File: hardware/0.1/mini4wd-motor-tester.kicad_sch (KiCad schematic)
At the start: 93 parts, among them J1 USB_C_Receptacle_USB2.0_16P, J2 JST SH, J3 JST SH, M1 Motor_DC, SW1 RA, SW2 RA, SW3 EC11, U1 TLV62130, U2 USBLC6-2SC6, U3 RT9080-33GJ5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

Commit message: add wheel rpm, aux 5V circuits
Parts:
- added C24: 100n, Capacitor_SMD:C_0603_1608Metric, symbol Device:C
- added D3: B5819W, Diode_SMD:D_SOD-123, symbol Device:D_Schottky
- added J4: JST XH, Connector_JST:JST_XH_B2B-XH-A_1x02_P2.50mm_Vertical, symbol Connector_Generic:Conn_01x02
- added Q2: AO3401A, Package_TO_SOT_SMD:SOT-23, symbol Transistor_FET:AO3401A
- added Q3: 2N7002, Package_TO_SOT_SMD:SOT-23, symbol Transistor_FET:Q_NMOS_GSD
- added R25: 22R, Resistor_SMD:R_0603_1608Metric, symbol Device:R
- added R26: 2K2, Resistor_SMD:R_0603_1608Metric, symbol Device:R
- added R27, R28: 10K, Resistor_SMD:R_0603_1608Metric, symbol Device:R
- added RV2: POT_10K, josh-passives-smt:Potentiometer_Bourns_TC33X_Vertical, symbol Device:R_Potentiometer
- added TP12: TP, TestPoint:TestPoint_Pad_D1.0mm, symbol Connector:TestPoint
- added U10: GP2S700HCP, josh-passives-smt:Sharp_GP2S700HCP, symbol Sensor_Proximity:GP2S700HCP
- C1, C23, C3: footprint Capacitor_SMD:C_1206_3216Metric -> Capacitor_SMD:C_0805_2012Metric; LCSC C13585 -> C440198; MPN  CL31A106KBHNNNE -> GRM21BR61H106KE43L; Manufacturer Samsung Electro-Mechanics -> Murata
- C2, C20, C21: Manufacturer FH (Guangdong Fenghua Advanced Tech) -> FH (Guangdong Fenghua Advanced Tech)
- J2, J3: Manufacturer JST Sales America -> JST
- L1: LCSC C3222743 -> C436515; MPN  IHLP1616BZER2R2M5A -> PSPMAA0402-2R2M-ANP; Manufacturer Vishay -> PROD Tech
- U9: footprint Package_SON:WSON-8-1EP_2x2mm_P0.5mm_EP0.9x1.6mm_ThermalVias -> Package_SON:WSON-8-1EP_2x2mm_P0.5mm_EP0.9x1.6mm
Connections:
- net +3V3: now also R26.1, U10.4 (A)
- net +5V: now also Q2.2 (S), R28.2
- net GND: now also C24.2, D3.2 (A), J4.2 (Pin_2), Q3.2 (S), R25.1, R27.2, RV2.3, U10.1
- net AUX_5V_EN: now reaches U5.38 (IO2)
- net AUX_5V_EN: now also Q3.1 (G), R27.1
- net WHEEL_OUT: now reaches U5.39 (IO1)
- net WHEEL_OUT: now also RV2.2, TP12.1
- net RPM_OUT renamed MOTOR_OUT
- new net: Q2.1 (G), Q3.3 (D), R28.1
- new net: C24.1, D3.1 (K), J4.1 (Pin_1), Q2.3 (D)
- new net: R26.2, RV2.1, U10.2
- new net: R25.2, U10.3 (K)
- no-connect marks 21 -> 19
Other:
- note added: "AUX 5V Supply"
- note added: "Motor RPM Counter"
- note added: "Wheel RPM Counter"
- note removed: "RPM Counter"
- moved on the sheet: TP11

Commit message: update motor cutout, provision space for wheel speed tester
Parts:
- R8: value 22K -> 30K; LCSC C31850 -> C22984; MPN  0603WAF2202T5E -> 0603WAF3002T5E
- R9: value 75K -> 100K; LCSC C23242 -> C25803; MPN  0603WAF7502T5E -> 0603WAF1003T5E

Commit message: shrinking board down
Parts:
- removed C18: 1u, Capacitor_SMD:C_0603_1608Metric, symbol Device:C
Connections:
- net TXD: now reaches J2.3 (Pin_3), U5.37 (TXD0)
- net RXD: now reaches J2.4 (Pin_4), U5.36 (RXD0)
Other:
- moved on the sheet: TP10, TP9
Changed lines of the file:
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@@
 	)
 	(junction
-		(at 247.65 31.75)
-		(diameter 0)
-		(color 0 0 0 0)
-	)
-	(junction
 		(at 358.14 208.28)
 		(diameter 0)
@@
 	(wire
 		(pts
+			(xy 199.39 45.72) (xy 209.55 45.72)
+		)
+		(stroke
+			(width 0)
+			(type default)
+		)
+	)
+	(wire
+		(pts
 			(xy 36.83 113.03) (xy 59.69 113.03)
 		)
@@
 	(wire
 		(pts
-			(xy 370.84 49.53) (xy 389.89 49.53)
+			(xy 370.84 49.53) (xy 391.16 49.53)
 		)
 		(stroke
@@
 	(wire
 		(pts
-			(xy 209.55 45.72) (xy 199.39 45.72)
-		)
-		(stroke
-			(width 0)
-			(type default)
-		)
-	)
-	(wire
-		(pts
 			(xy 54.61 35.56) (xy 50.8 35.56)
 		)
@@
 	(wire
 		(pts
-			(xy 370.84 44.45) (xy 389.89 44.45)
+			(xy 370.84 44.45) (xy 391.16 44.45)
 		)
 		(stroke
@@
 	(wire
 		(pts
-			(xy 260.35 31.75) (xy 260.35 34.29)
-		)
-		(stroke
-			(width 0)
-			(type default)
-		)
-	)
-	(wire
-		(pts
 			(xy 73.66 46.99) (xy 73.66 45.72)
 		)
@@
 	(wire
 		(pts
-			(xy 247.65 31.75) (xy 260.35 31.75)
-		)
-		(stroke
-			(width 0)
-			(type default)
-		)
-	)
-	(wire
-		(pts
 			(xy 278.13 196.85) (xy 278.13 198.12)
 		)
@@
 		)
 	)
+	(label "RXD"
+		(at 201.93 48.26 0)
+		(effects
+			(font
+				(size 1.27 1.27)
+				(thickness 0.254)
+				(bold yes)
+			)
+			(justify left bottom)
+		)
+	)
 	(label "I2C_SDA"
 		(at 256.54 71.12 180)
@@
 		)
 	)
+	(label "TXD"
+		(at 201.93 45.72 0)
+		(effects
+			(font
+				(size 1.27 1.27)
+				(thickness 0.254)
+				(bold yes)
+			)
+			(justify left bottom)
+		)
+	)
 	(label "SPI_POCI"
 		(at 256.54 83.82 180)
@@
 	(symbol
 		(lib_id "Connector:TestPoint")
-		(at 389.89 44.45 270)
+		(at 391.16 44.45 270)
 		(mirror x)
 		(unit 1)
@@
 		(dnp no)
 		(property "Reference" "TP9"
-			(at 390.652 43.434 90)
+			(at 391.922 43.434 90)
 			(effects
 				(font
@@
 		)
 		(property "Value" "TP"
-			(at 391.16 45.72 90)
+			(at 392.43 45.72 90)
 			(effects
 				(font
@@
 		)
 		(property "Footprint" "TestPoint:TestPoint_Pad_D1.0mm"
-			(at 389.89 39.37 0)
+			(at 391.16 39.37 0)
 			(effects
 				(font
@@
 		)
 		(property "Datasheet" "~"
-			(at 389.89 39.37 0)
+			(at 391.16 39.37 0)
 			(effects
 				(font
@@
 		)
 		(property "Description" "test point"
-			(at 389.89 44.45 0)
+			(at 391.16 44.45 0)
 			(effects
 				(font
@@
 		)
 		(property "Value" "RA"
-			(at 254 38.862 90)
+			(at 252.476 38.862 90)
 			(effects
 				(font
@@
 	)
 	(symbol
-		(lib_id "Device:C")
-		(at 260.35 38.1 180)
-		(unit 1)
-		(exclude_from_sim no)
-		(in_bom yes)
-		(on_board yes)
-		(dnp no)
-		(property "Reference" "C18"
-			(at 263.271 36.9316 0)
-			(effects
-				(font
-					(size 1.27 1.27)
-				)
-				(justify right)
-			)
-		)
-		(property "Value" "1u"
-			(at 263.271 39.243 0)
-			(effects
-				(font
-					(size 1.27 1.27)
-				)
-				(justify right)
-			)
-		)
-		(property "Footprint" "Capacitor_SMD:C_0603_1608Metric"
-			(at 259.3848 34.29 0)
-			(effects
-				(font
-					(size 1.27 1.27)
-				)
-				(hide yes)
-			)
-		)
-		(property "Datasheet" "~"
-			(at 260.35 38.1 0)
-			(effects
-				(font
-					(size 1.27 1.27)
-				)
-				(hide yes)
-			)
-		)
-		(property "Description" ""
-			(at 260.35 38.1 0)
-			(effects
-				(font
-					(size 1.27 1.27)
-				)
-			)
-		)
-		(property "LCSC" "C15849"
-			(at 260.35 38.1 0)
-			(effects
-				(font
-					(size 1.27 1.27)
-				)
-				(hide yes)
-			)
-		)
-		(property "Manufacturer" "Samsung Electro-Mechanics"
-			(at 260.35 38.1 0)
-			(effects
-				(font
-					(size 1.27 1.27)
-				)
-				(hide yes)
-			)
-		)
-		(property "MPN " "CL10A105KB8NNNC"
-			(at 260.35 38.1 0)
-			(effects
-				(font
-					(size 1.27 1.27)
-				)
-				(hide yes)
-			)
-		)
-		(pin "2"
-		)
-		(pin "1"
-		)
-		(instances
-			(project "mini4x4-motor-tester"
-				(path "/5d80fb7d-ae13-4e08-ba61-7e26fe6662ad"
-					(reference "C18")
-					(unit 1)
-				)
-			)
-		)
-	)
-	(symbol
 		(lib_id "Device:R")
 		(at 384.81 73.66 0)
@@
 	(symbol
 		(lib_id "Connector:TestPoint")
-		(at 389.89 49.53 270)
+		(at 391.16 49.53 270)
 		(mirror x)
 		(unit 1)
@@
 		(dnp no)
 		(property "Reference" "TP10"
-			(at 390.906 48.514 90)
+			(at 391.414 48.514 90)
 			(effects
 				(font
@@
 		)
 		(property "Value" "TP"
-			(at 391.16 50.8 90)
+			(at 392.43 50.8 90)
 			(effects
 				(font
@@
 		)
 		(property "Footprint" "TestPoint:TestPoint_Pad_D1.0mm"
-			(at 389.89 44.45 0)
+			(at 391.16 44.45 0)
 			(effects
 				(font
@@
 		)
 		(property "Datasheet" "~"
-			(at 389.89 44.45 0)
+			(at 391.16 44.45 0)
 			(effects
 				(font
@@
 		)
 		(property "Description" "test point"
-			(at 389.89 49.53 0)
+			(at 391.16 49.53 0)
 			(effects
 				(font
@@
 					(unit 1)
 				)
-			)
-		)
-	)
-	(symbol
-		(lib_id "power:GND")
-		(at 260.35 41.91 0)
-		(unit 1)
-		(exclude_from_sim no)
-		(in_bom yes)
-		(on_board yes)
-		(dnp no)
-		(property "Reference" "#PWR048"
-			(at 260.35 48.26 0)
-			(effects
-				(font
-					(size 1.27 1.27)
-				)
-				(hide yes)
-			)
-		)
-		(property "Value" "GND"
-			(at 260.477 46.3042 0)
-			(effects
-				(font
-					(size 1.27 1.27)
-				)
-			)
-		)
-		(property "Footprint" ""
-			(at 260.35 41.91 0)
-			(effects
-				(font
-					(size 1.27 1.27)
-				)
-				(hide yes)
-			)
-		)
-		(property "Datasheet" ""
-			(at 260.35 41.91 0)
-			(effects
-				(font
-					(size 1.27 1.27)
-				)
-				(hide yes)
-			)
-		)
-		(property "Description" "Power symbol creates a global label with name \"GND\" , ground"
-			(at 260.35 41.91 0)
-			(effects
-				(font
-					(size 1.27 1.27)
-				)
-				(hide yes)
-			)
-		)
-		(pin "1"
-		)
-		(instances
-			(project "mini4x4-motor-tester"
-				(path "/5d80fb7d-ae13-4e08-ba61-7e26fe6662ad"
-					(reference "#PWR048")
-					(unit 1)
-				)

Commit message: rough placement of all parts on smaller board
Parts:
- removed C24: 100n, Capacitor_SMD:C_0603_1608Metric, symbol Device:C
- removed FID4, FID5, FID6: Fiducial, Fiducial:Fiducial_1mm_Mask3mm, symbol Mechanical:Fiducial
- added TP13: TP, TestPoint:TestPoint_Pad_D1.0mm, symbol Connector:TestPoint
- C12: value 100n -> 1u; LCSC C14663 -> C15849; MPN  CC0603KRX7R9BB104 -> CL10A105KB8NNNC
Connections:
- net +3V3: now also C12.2, R6.1; no longer C12.1
- net +VMOT: no longer R6.1
- net GND: now also C12.1; no longer C12.2
- net at R6.2, U1.4 (PG): now also TP13.1
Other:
- moved on the sheet: FID1, FID2, FID3, H1, H2, H3, H4, R6

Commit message: I think the final form has been reached?
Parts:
- added G1: ~, josh-logos:josh-details, symbol Mechanical:Mechanical_Shape
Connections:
- net GND: now also J4.1 (Pin_1); no longer J4.2 (Pin_2)
- net at D3.1 (K), Q2.3 (D): now also J4.2 (Pin_2); no longer J4.1 (Pin_1)

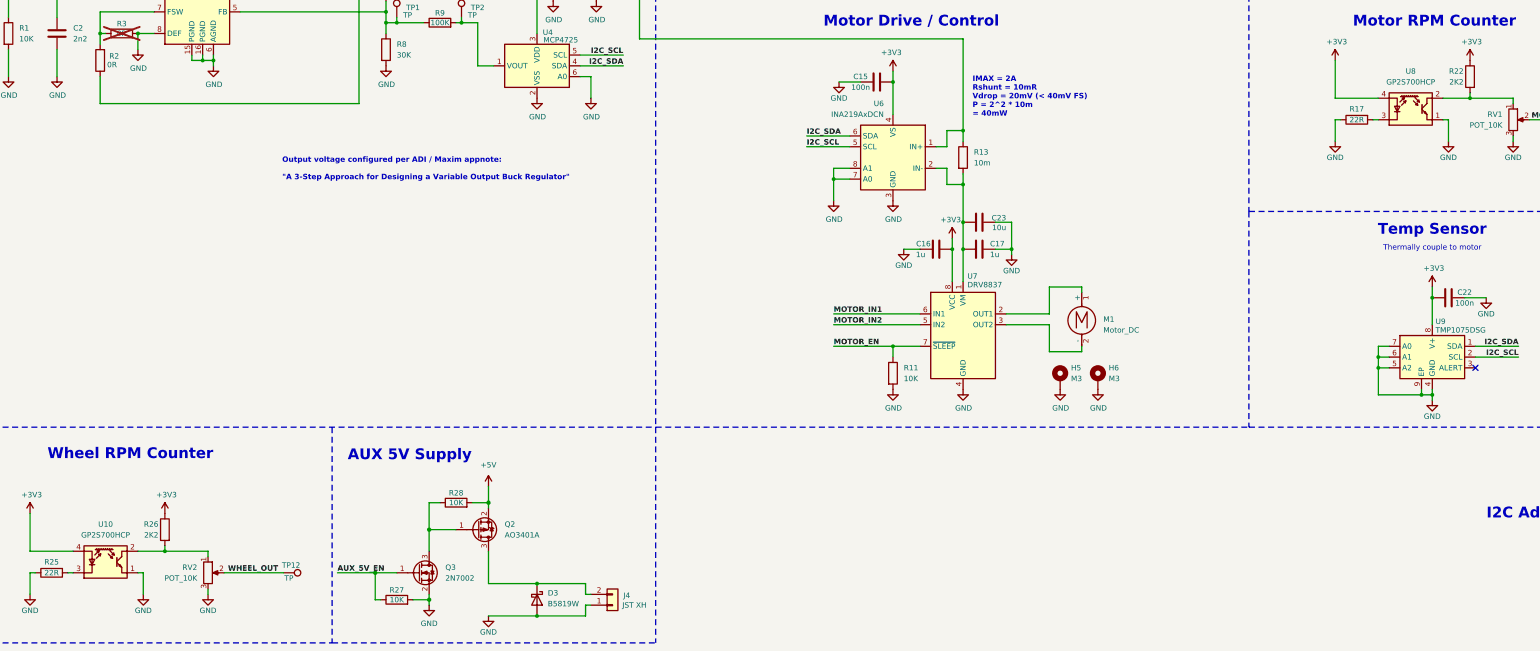
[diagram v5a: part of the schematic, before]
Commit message: change opto, move motor lower
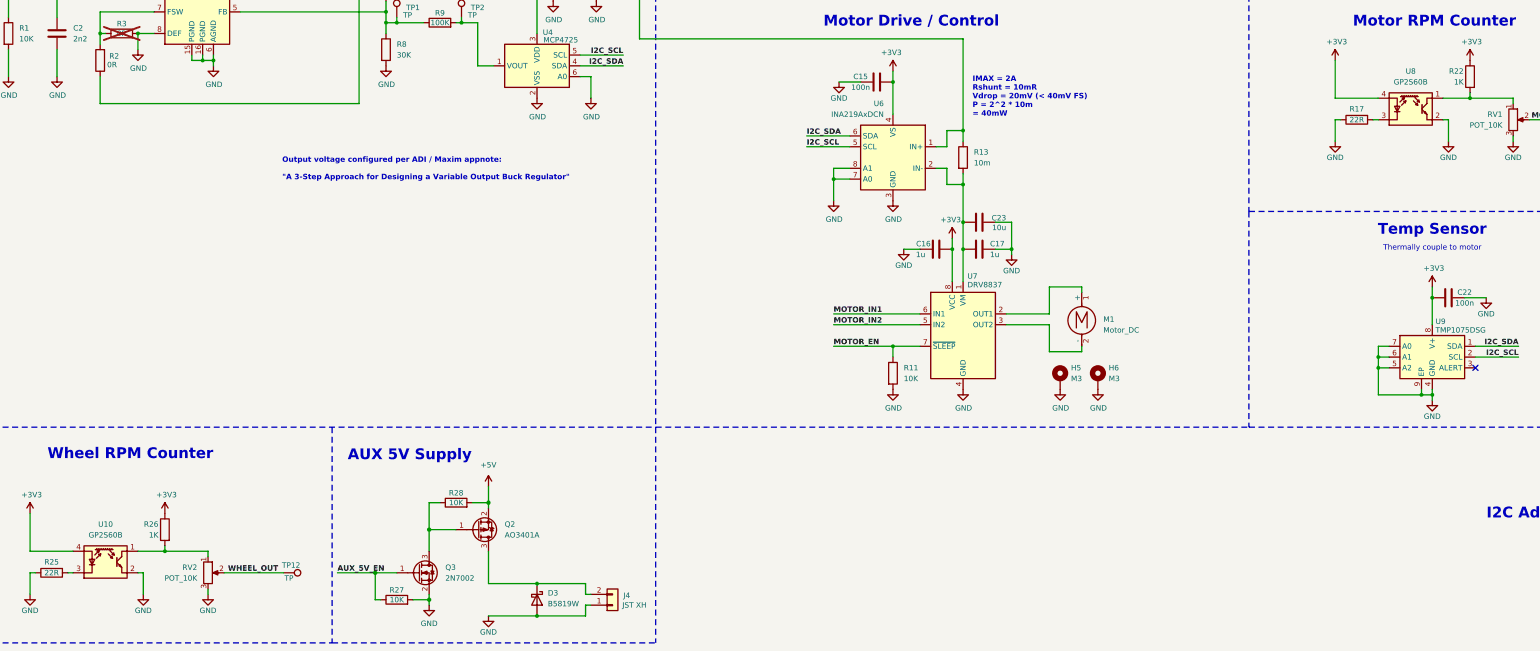
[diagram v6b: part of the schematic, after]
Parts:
- removed U10, U8: GP2S700HCP, josh-passives-smt:Sharp_GP2S700HCP, symbol Sensor_Proximity:GP2S700HCP
- added U10, U8: GP2S60B, josh-passives-smt:Sharp_GP2S60B, symbol josh-led:GP2S60B
- Q2: LCSC (none) -> C15127; MPN  (none) -> AO3401A; Manufacturer (none) -> Alpha & Omega Semicon
- R22, R26: value 2K2 -> 1K; LCSC C4190 -> C21190; MPN  0603WAF2201T5E -> 0603WAF1001T5E
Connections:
- net +3V3: now also U10.4 (A), U8.4 (A)
- net GND: now also U10.2, U8.2
- net at R17.2: now also U8.3 (K)
- net at R22.2, RV1.1: now also U8.1
- net at R26.2, RV2.1: now also U10.1
- net at R25.2: now also U10.3 (K)
